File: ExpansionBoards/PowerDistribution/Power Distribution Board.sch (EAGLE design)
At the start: 28 parts, among them J1 216571-2002, J10 640445-6, J11 640445-6, J12 640445-2, J13 640445-5, J14 640445-3, J15 216571-2003, J16 640445-8, J2 216571-2005, J3 216571-2005, J4 350211-1, J5 206832-1001, J7 216571-2003, J8 350211-1, J9 640445-6, K1 AHQSS105DM2FA0G, U3 LM338T/NOPB

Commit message: exp board: power distribution: 24-pin ATX connector, 48V interlock via MOSFET, Always On jumper options
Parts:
- added J17: 640445-8, SamacSys_Parts:640445-8
- added J6: 44206-0007, SamacSys_Parts:44206-0007
- added LED2: Red, led:LED5MM
- added LED3: Yellow, led:LED5MM
- added LED4: Green, led:LED5MM
- added LED5: Orange, led:LED5MM
- added OK1: PC817, optocoupler:PC817
- added Q1: 2N2222A, SamacSys_Parts:2N2222A
- added Q2: IRF9530, transistor-power:IRF9530
- added R10: 1.1K 1/2W, rcl:R-US_0309/12
- added R11: 220R, rcl:R-US_0309/12
- added R4: 270R, rcl:R-US_0204/7
- added R5: 470R, rcl:R-US_0204/7
- added R6: 8.2K, rcl:R-US_0207/10
- added R7: 2.2K, rcl:R-US_0207/10
- added R8: 150R, rcl:R-US_0309/12
- added R9: 510R 1/4W, rcl:R-US_0309/12
- added W1, W2: JUMPER-WIRE, SamacSys_Parts:JUMPER-WIRE
- J1: value 216571-2002 -> 216571-2005; device SamacSys_Parts:216571-2002 -> SamacSys_Parts:216571-2005
- J12: value 640445-2 -> 640445-6; device SamacSys_Parts:640445-2 -> SamacSys_Parts:640445-6
- J13: value 640445-5 -> 640445-2; device SamacSys_Parts:640445-5 -> SamacSys_Parts:640445-2
- J14: value 640445-3 -> 640445-5; device SamacSys_Parts:640445-3 -> SamacSys_Parts:640445-5
- J15: value 216571-2003 -> 640445-3; device SamacSys_Parts:216571-2003 -> SamacSys_Parts:640445-3
- J16: value 640445-8 -> 216571-2003; device SamacSys_Parts:640445-8 -> SamacSys_Parts:216571-2003
- J2: value 216571-2005 -> 216571-2002; device SamacSys_Parts:216571-2005 -> SamacSys_Parts:216571-2002
- J4: value 350211-1 -> 216571-2005; device SamacSys_Parts:350211-1 -> SamacSys_Parts:216571-2005
- J5: value 206832-1001 -> 216571-2005; device SamacSys_Parts:206832-1001 -> SamacSys_Parts:216571-2005
- J7: value 216571-2003 -> 216571-2004; device SamacSys_Parts:216571-2003 -> SamacSys_Parts:216571-2004
- J8: value 350211-1 -> 216571-2003; device SamacSys_Parts:350211-1 -> SamacSys_Parts:216571-2003
- J9: value 640445-6 -> 350211-1; device SamacSys_Parts:640445-6 -> SamacSys_Parts:350211-1
- LED1: value (none) -> Blue
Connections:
- new net -12V: J6.14
- new net 3V3: J6.1, J6.13, J6.2
- new net 3V3_1: J6.12
- new net 5V_STANDBY: J6.9
- new net N$10: LED3.A, R9.1
- new net N$11: LED4.A, R10.1
- new net N$12: LED5.A, R11.1
- new net N$2: Q2.D, RT1.1
- new net N$5: Q2.G, R6.1, R7.2
- new net N$6: Q1.C, R6.2
- new net N$7: Q1.B, R5.1
- new net N$8: J2.2, R5.2
- new net N$9: LED2.A, R8.1
- new net PS_ON#: J6.16, OK1.COL, W1.P$2
- new net PWR_OK: J6.8
- net 12V: now also J11.5, J14.1, J14.2, J14.3, J14.4, J14.5, J4.2, J6.10, J6.11, R9.2; no longer J13.1, J13.2, J13.3, J13.4, J13.5, J4.1, J5.2, J9.5
- net 12VPC: now also J9.1; no longer J8.1
- net 24V: now also J15.1, J15.2, J15.3, R10.2; no longer J14.1, J14.2, J14.3
- net 48V: now also J16.1, J16.2, J16.3; no longer J15.1, J15.2, J15.3
- net 5V: now also J12.1, J12.2, J12.3, J12.4, J12.5, J12.6, J2.1, J5.2, J6.21, J6.22, J6.23, J6.4, J6.6, R8.2; no longer J11.1, J11.2, J11.3, J11.4, J11.5, J4.4, J5.7, J9.6
- net 5VPC: now also J9.4, R4.2; no longer J8.4
- net 6V3: now also J13.1, J13.2, R11.2; no longer J12.1, J12.2
- net GND: now also J1.1, J1.3, J11.1, J11.2, J11.3, J11.4, J17.1, J17.2, J17.3, J17.4, J17.5, J17.6, J17.7, J17.8, J4.1, J6.15, J6.17, J6.18, J6.19, J6.24, J6.3, J6.5, J6.7, LED2.C, LED3.C, LED4.C, LED5.C, OK1.C, OK1.EMIT, Q1.E, W1.P$1; no longer J16.1, J16.2, J16.3, J16.4, J16.5, J16.6, J16.7, J16.8, J2.1, J2.3, J4.2, J5.6, J5.8, J8.3, J9.1, J9.4
- net LINE_HOT: now also J1.5, J4.5, J7.3, W2.P$2; no longer J1.1, J5.10
- net LINE_HOT_IN: now also J8.3, W2.P$1; no longer J7.3
- net LINE_NEUTRAL: now also J1.4, J4.4, J8.1; no longer J2.4, J5.9
- net N$1: now also J1.2, Q2.S, R7.1; no longer J2.2, RT1.1
- net N$4: now also OK1.A, R4.1; no longer J1.2, J2.5
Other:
- note added: "** WARNING ** WARNING ** WARNING ** Connect only ONE of 5V/12V SMPS **OR** Secondary ATX power supply unit. The 5V and 12V rails are connected to both headers, so connecting both types of power supplies simultaneously will create a dangerous interconnection where each supply tries to drive the other. The reason both headers are provided is only to allow the user to decide which type of 5V/12V sup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"
- note added: "+48V DC"
- note added: "120VAC SWITCHED MAINS OUT This can be connected as the power input to a power strip, to provide switched power to external devices (TVs/monitors, audio amp)."
- note added: "12V INDICATOR"
- note added: "12V SMPS"
- note added: "24V INDICATOR"
- note added: "5V INDICATOR"
- note added: "5V SMPS"
- note added: "6.3V INDICATOR"
- note added: "ALWAYS ON OPTION To bypass PSU switching for ALWAYS ON operation, - Install jumper wires W1, W2 - DO NOT POPULATE K1, OK1, R4"
- note added: "COIN DOOR INTERLOCK 5V control signal to coin door switch activates 2N2222 when switch is closed, which in turn activates P-MOSFET to control 48VDC power."
- note added: "Generic 5mm Blue LED Vf approx 3.2V, If 20mA Serves as indicator, and drains caps when power is off."
- note added: "Generic 5mm green LED, Vf 2.1V, If 20mA"
- note added: "Generic 5mm orange LED, Vf 2V, If 20mA"
- note added: "Generic 5mm red LED, Vf 2.1V, If 20mA"
- note added: "Generic 5mm yellow LED, Vf 2V, If 20mA"
- note added: "NOTE: Connect the ATX supply's 120VAC line in directly to mains. The power distribution board will provide "soft" power control via PS_ON#."
- note added: "SECONDARY ATX POWER CONTROL Grounds PS_ON# when PC is on."
- note removed: "5V/12V SMPS"
- note removed: "COIN DOOR INTERLOCK"
- note removed: "Generic 5mm LED Vf approx 3.2V, If 20mA Indicator + drains caps when power is off"
- note removed: "SMPS Connections These connectors route switched mains power to the secondary power supplies, and route the DC output of the power back to the distribution board."

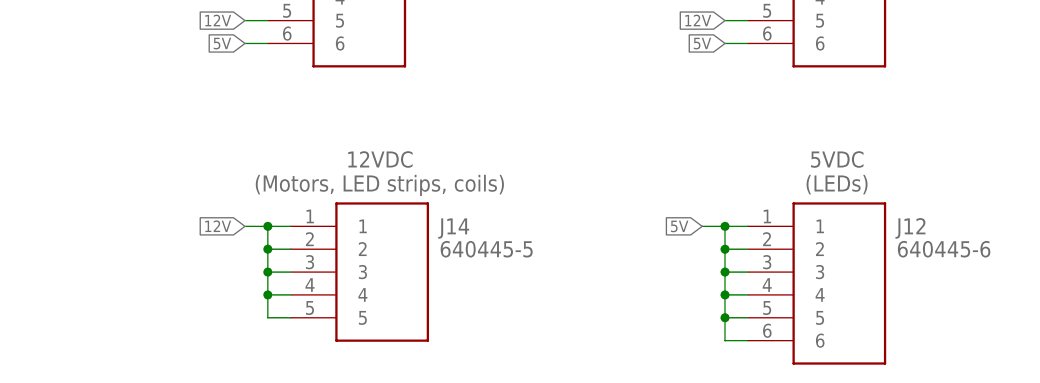
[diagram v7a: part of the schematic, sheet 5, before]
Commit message: exp board: power distro board tweaks
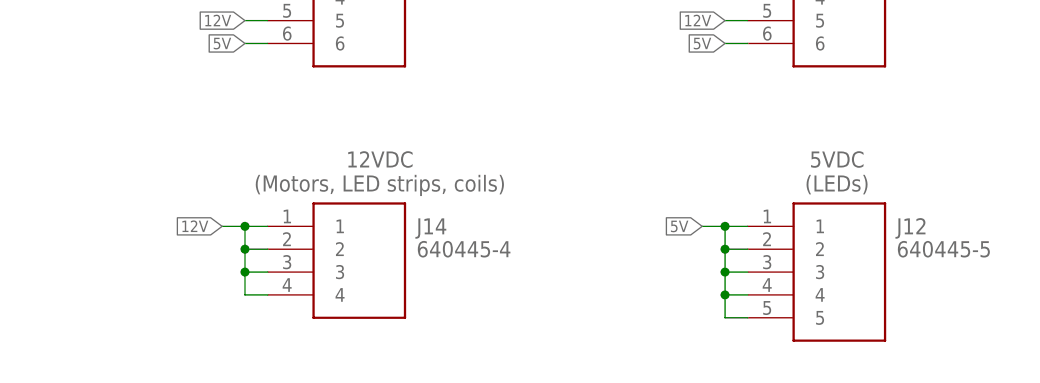
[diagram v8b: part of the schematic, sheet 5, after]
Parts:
- J12: value 640445-6 -> 640445-5; device SamacSys_Parts:640445-6 -> SamacSys_Parts:640445-5
- J14: value 640445-5 -> 640445-4; device SamacSys_Parts:640445-5 -> SamacSys_Parts:640445-4
- R1: value 2.4K/1W -> 2.4K 1W
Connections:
- net 12V: no longer J14.5
- net 5V: no longer J12.6
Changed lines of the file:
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@@
 <part name="J13" library="SamacSys_Parts" deviceset="640445-2" device=""/>
 <part name="J15" library="SamacSys_Parts" deviceset="640445-3" device=""/>
-<part name="J14" library="SamacSys_Parts" deviceset="640445-5" device=""/>
-<part name="J12" library="SamacSys_Parts" deviceset="640445-6" device=""/>
 <part name="J10" library="SamacSys_Parts" deviceset="640445-6" device=""/>
 <part name="J8" library="SamacSys_Parts" deviceset="216571-2003" device=""/>
 <part name="J11" library="SamacSys_Parts" deviceset="640445-6" device=""/>
 <part name="LED1" library="led" deviceset="LED" device="5MM" value="Blue"/>
-<part name="R1" library="rcl" deviceset="R-US_" device="0309/12" value="2.4K/1W"/>
+<part name="R1" library="rcl" deviceset="R-US_" device="0309/12" value="2.4K 1W"/>
 <part name="D1" library="diode" deviceset="1N4007" device=""/>
 <part name="J6" library="SamacSys_Parts" deviceset="44206-0007" device=""/>
@@
 <part name="J4" library="SamacSys_Parts" deviceset="216571-2005" device=""/>
 <part name="J5" library="SamacSys_Parts" deviceset="216571-2005" device=""/>
+<part name="J12" library="SamacSys_Parts" deviceset="640445-5" device=""/>
+<part name="J14" library="SamacSys_Parts" deviceset="640445-4" device=""/>
 </parts>
 <sheets>
@@
 <attribute name="VALUE" x="97.79" y="17.78" size="1.778" layer="96" align="center-left"/>
 </instance>
-<instance part="J14" gate="G$1" x="154.94" y="20.32" smashed="yes">
-<attribute name="NAME" x="171.45" y="20.32" size="1.778" layer="95" align="center-left"/>
-<attribute name="VALUE" x="171.45" y="17.78" size="1.778" layer="96" align="center-left"/>
+<instance part="J10" gate="G$1" x="152.4" y="53.34" smashed="yes">
+<attribute name="NAME" x="168.91" y="53.34" size="1.778" layer="95" align="center-left"/>
+<attribute name="VALUE" x="168.91" y="50.8" size="1.778" layer="96" align="center-left"/>
+</instance>
+<instance part="J11" gate="G$1" x="205.74" y="53.34" smashed="yes">
+<attribute name="NAME" x="222.25" y="53.34" size="1.778" layer="95" align="center-left"/>
+<attribute name="VALUE" x="222.25" y="50.8" size="1.778" layer="96" align="center-left"/>
 </instance>
 <instance part="J12" gate="G$1" x="205.74" y="20.32" smashed="yes">
@@
 <attribute name="VALUE" x="222.25" y="17.78" size="1.778" layer="96" align="center-left"/>
 </instance>
-<instance part="J10" gate="G$1" x="152.4" y="53.34" smashed="yes">
-<attribute name="NAME" x="168.91" y="53.34" size="1.778" layer="95" align="center-left"/>
-<attribute name="VALUE" x="168.91" y="50.8" size="1.778" layer="96" align="center-left"/>
-</instance>
-<instance part="J11" gate="G$1" x="205.74" y="53.34" smashed="yes">
-<attribute name="NAME" x="222.25" y="53.34" size="1.778" layer="95" align="center-left"/>
-<attribute name="VALUE" x="222.25" y="50.8" size="1.778" layer="96" align="center-left"/>
+<instance part="J14" gate="G$1" x="152.4" y="20.32" smashed="yes">
+<attribute name="NAME" x="168.91" y="20.32" size="1.778" layer="95" align="center-left"/>
+<attribute name="VALUE" x="168.91" y="17.78" size="1.778" layer="96" align="center-left"/>
 </instance>
 </instances>
@@
 </segment>
 <segment>
-<pinref part="J12" gate="G$1" pin="1"/>
 <wire x1="200.66" y1="20.32" x2="203.2" y2="20.32" width="0.1524" layer="91"/>
 <wire x1="203.2" y1="20.32" x2="205.74" y2="20.32" width="0.1524" layer="91"/>
 <wire x1="203.2" y1="20.32" x2="203.2" y2="17.78" width="0.1524" layer="91"/>
 <junction x="203.2" y="20.32"/>
-<pinref part="J12" gate="G$1" pin="6"/>
 <wire x1="203.2" y1="17.78" x2="203.2" y2="15.24" width="0.1524" layer="91"/>
 <wire x1="203.2" y1="15.24" x2="203.2" y2="12.7" width="0.1524" layer="91"/>
 <wire x1="203.2" y1="12.7" x2="203.2" y2="10.16" width="0.1524" layer="91"/>
-<wire x1="203.2" y1="10.16" x2="203.2" y2="7.62" width="0.1524" layer="91"/>
-<wire x1="203.2" y1="7.62" x2="205.74" y2="7.62" width="0.1524" layer="91"/>
-<pinref part="J12" gate="G$1" pin="5"/>
 <wire x1="203.2" y1="10.16" x2="205.74" y2="10.16" width="0.1524" layer="91"/>
-<junction x="203.2" y="10.16"/>
-<pinref part="J12" gate="G$1" pin="4"/>
 <wire x1="203.2" y1="12.7" x2="205.74" y2="12.7" width="0.1524" layer="91"/>
 <junction x="203.2" y="12.7"/>
-<pinref part="J12" gate="G$1" pin="3"/>
 <wire x1="203.2" y1="15.24" x2="205.74" y2="15.24" width="0.1524" layer="91"/>
 <junction x="203.2" y="15.24"/>
-<pinref part="J12" gate="G$1" pin="2"/>
 <wire x1="203.2" y1="17.78" x2="205.74" y2="17.78" width="0.1524" layer="91"/>
 <junction x="203.2" y="17.78"/>
 <label x="200.66" y="20.32" size="1.27" layer="95" rot="R180" xref="yes"/>
+<pinref part="J12" gate="G$1" pin="1"/>
+<pinref part="J12" gate="G$1" pin="2"/>
+<pinref part="J12" gate="G$1" pin="3"/>
+<pinref part="J12" gate="G$1" pin="4"/>
+<pinref part="J12" gate="G$1" pin="5"/>
 </segment>
 <segment>
@@
 </segment>
 <segment>
+<wire x1="147.32" y1="20.32" x2="149.86" y2="20.32" width="0.1524" layer="91"/>
+<wire x1="149.86" y1="20.32" x2="152.4" y2="20.32" width="0.1524" layer="91"/>
+<wire x1="149.86" y1="20.32" x2="149.86" y2="17.78" width="0.1524" layer="91"/>
+<junction x="149.86" y="20.32"/>
+<wire x1="149.86" y1="17.78" x2="152.4" y2="17.78" width="0.1524" layer="91"/>
+<wire x1="149.86" y1="17.78" x2="149.86" y2="15.24" width="0.1524" layer="91"/>
+<junction x="149.86" y="17.78"/>
+<wire x1="149.86" y1="15.24" x2="152.4" y2="15.24" width="0.1524" layer="91"/>
+<wire x1="149.86" y1="15.24" x2="149.86" y2="12.7" width="0.1524" layer="91"/>
+<junction x="149.86" y="15.24"/>
+<wire x1="149.86" y1="12.7" x2="152.4" y2="12.7" width="0.1524" layer="91"/>
+<label x="147.32" y="20.32" size="1.27" layer="95" rot="R180" xref="yes"/>
 <pinref part="J14" gate="G$1" pin="1"/>
-<wire x1="149.86" y1="20.32" x2="152.4" y2="20.32" width="0.1524" layer="91"/>
-<wire x1="152.4" y1="20.32" x2="154.94" y2="20.32" width="0.1524" layer="91"/>
-<wire x1="152.4" y1="20.32" x2="152.4" y2="17.78" width="0.1524" layer="91"/>
-<junction x="152.4" y="20.32"/>
 <pinref part="J14" gate="G$1" pin="2"/>
-<wire x1="152.4" y1="17.78" x2="154.94" y2="17.78" width="0.1524" layer="91"/>
-<wire x1="152.4" y1="17.78" x2="152.4" y2="15.24" width="0.1524" layer="91"/>
-<junction x="152.4" y="17.78"/>
 <pinref part="J14" gate="G$1" pin="3"/>
-<wire x1="152.4" y1="15.24" x2="154.94" y2="15.24" width="0.1524" layer="91"/>
-<wire x1="152.4" y1="15.24" x2="152.4" y2="12.7" width="0.1524" layer="91"/>
-<junction x="152.4" y="15.24"/>
 <pinref part="J14" gate="G$1" pin="4"/>
-<wire x1="152.4" y1="12.7" x2="154.94" y2="12.7" width="0.1524" layer="91"/>
-<wire x1="152.4" y1="12.7" x2="152.4" y2="10.16" width="0.1524" layer="91"/>
-<junction x="152.4" y="12.7"/>
-<pinref part="J14" gate="G$1" pin="5"/>
-<wire x1="152.4" y1="10.16" x2="154.94" y2="10.16" width="0.1524" layer="91"/>
-<label x="149.86" y="20.32" size="1.27" layer="95" rot="R180" xref="yes"/>
-</segment>
-<segment>
+</segment>
+<segment>
